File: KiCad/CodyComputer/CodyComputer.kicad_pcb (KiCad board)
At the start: 2 copper layers, 160 x 100 mm, 59 parts, among them J1 Barrel_Jack, J2 Power LED, J3 PropPlug, J4 Video Out, J5 Audio Out, J6 Cody Expansion/Cartridge Port, J7 Keyboard Connector, J8 Joystick 1, J9 Joystick 2, U1 74HC541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

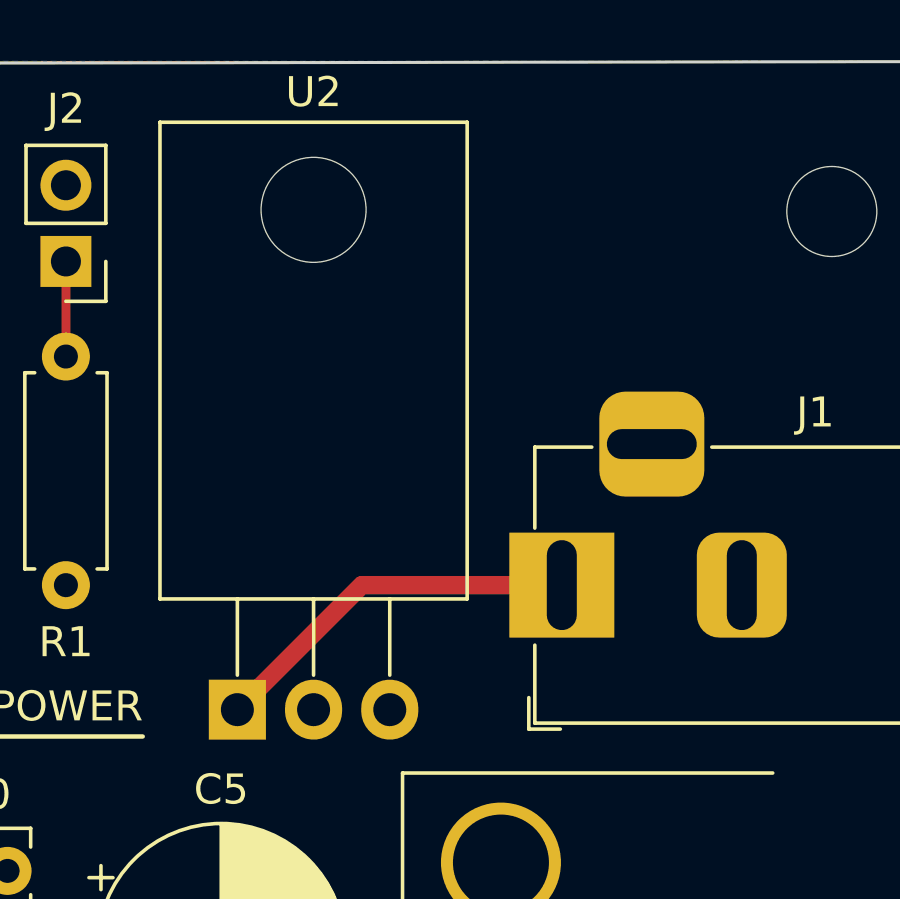
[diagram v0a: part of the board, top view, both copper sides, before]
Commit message: Add debug power connector to PCB
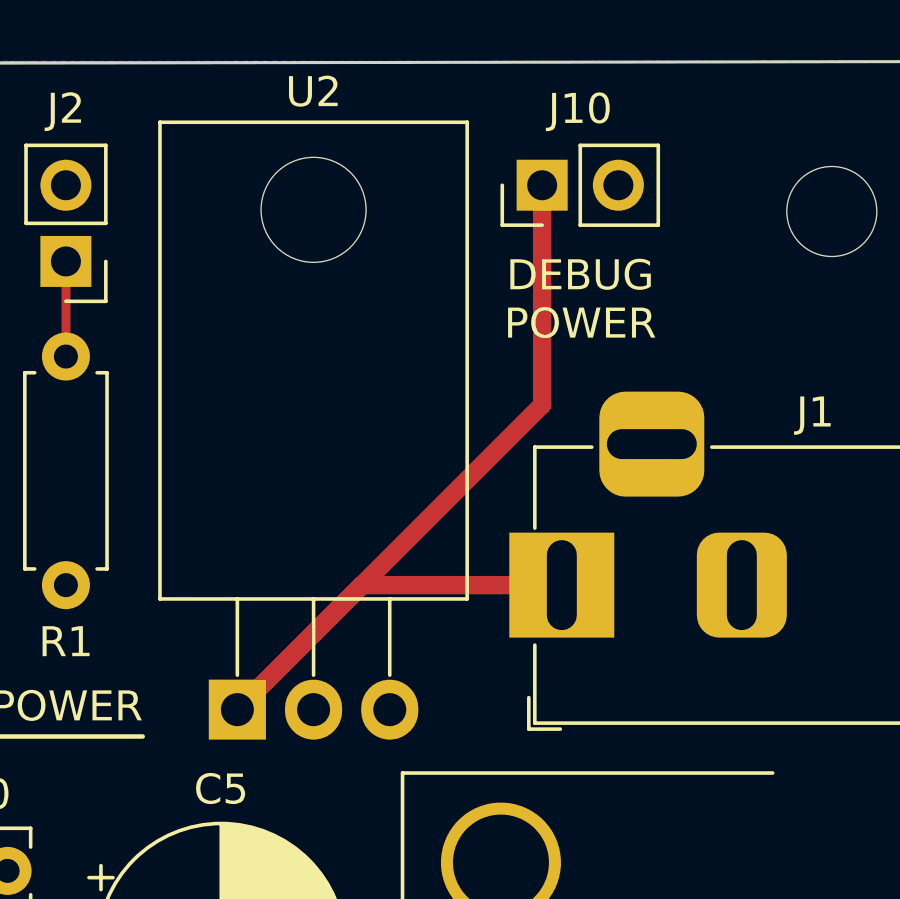
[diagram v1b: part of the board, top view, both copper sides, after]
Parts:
- added J10: Debug Power (Do Not Populate), Connector_PinHeader_2.54mm:PinHeader_1x02_P2.54mm_Vertical, F.Cu at (203.8, 51.4)
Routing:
- net /Propeller, Video, Audio, Power/VIN: track 12.5 -> 34.2 mm
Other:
- board text added: "DEBUG POWER"
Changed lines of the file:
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@@
     )
   )
+  (footprint "Connector_PinHeader_2.54mm:PinHeader_1x02_P2.54mm_Vertical" (layer "F.Cu")
+    (at 203.835 51.435 90)
+    (descr "Through hole straight pin header, 1x02, 2.54mm pitch, single row")
+    (tags "Through hole pin header THT 1x02 2.54mm single row")
+    (property "Sheetfile" "Propeller.kicad_sch")
+    (property "Sheetname" "Propeller, Video, Audio, Power")
+    (attr through_hole)
+    (fp_text reference "J10" (at 2.54 1.27 180) (layer "F.SilkS")
+      (effects (font (size 1 1) (thickness 0.15)))
+    )
+    (fp_text value "Debug Power (Do Not Populate)" (at -2.286 0.005 180) (layer "F.Fab")
+      (effects (font (size 1 1) (thickness 0.15)))
+    )
+    (fp_text user "${REFERENCE}" (at 0 1.27) (layer "F.Fab")
+      (effects (font (size 1 1) (thickness 0.15)))
+    )
+    (fp_line (start -1.33 1.27) (end 1.33 1.27) (layer "F.SilkS") (width 0.12))
+    (fp_line (start -1.33 3.87) (end 1.33 3.87) (layer "F.SilkS") (width 0.12))
+    (fp_line (start -1.33 -1.33) (end 0 -1.33) (layer "F.SilkS") (width 0.12))
+    (fp_line (start -1.33 0) (end -1.33 -1.33) (layer "F.SilkS") (width 0.12))
+    (fp_line (start -1.33 1.27) (end -1.33 3.87) (layer "F.SilkS") (width 0.12))
+    (fp_line (start 1.33 1.27) (end 1.33 3.87) (layer "F.SilkS") (width 0.12))
+    (fp_line (start 1.8 -1.8) (end -1.8 -1.8) (layer "F.CrtYd") (width 0.05))
+    (fp_line (start -1.8 -1.8) (end -1.8 4.35) (layer "F.CrtYd") (width 0.05))
+    (fp_line (start -1.8 4.35) (end 1.8 4.35) (layer "F.CrtYd") (width 0.05))
+    (fp_line (start 1.8 4.35) (end 1.8 -1.8) (layer "F.CrtYd") (width 0.05))
+    (fp_line (start -1.27 3.81) (end -1.27 -0.635) (layer "F.Fab") (width 0.1))
+    (fp_line (start -1.27 -0.635) (end -0.635 -1.27) (layer "F.Fab") (width 0.1))
+    (fp_line (start 1.27 -1.27) (end 1.27 3.81) (layer "F.Fab") (width 0.1))
+    (fp_line (start -0.635 -1.27) (end 1.27 -1.27) (layer "F.Fab") (width 0.1))
+    (fp_line (start 1.27 3.81) (end -1.27 3.81) (layer "F.Fab") (width 0.1))
+    (pad "1" thru_hole rect (at 0 0 90) (size 1.7 1.7) (drill 1) (layers *.Cu *.Mask)
+      (net 54 "/Propeller, Video, Audio, Power/VIN") (pinfunction "Pin_1") (pintype "passive"))
+    (pad "2" thru_hole oval (at 0 2.54 90) (size 1.7 1.7) (drill 1) (layers *.Cu *.Mask)
+      (net 16 "GND") (pinfunction "Pin_2") (pintype "passive"))
+    (model "${KICAD6_3DMODEL_DIR}/Connector_PinHeader_2.54mm.3dshapes/PinHeader_1x02_P2.54mm_Vertical.wrl"
+      (offset (xyz 0 0 0))
+      (scale (xyz 1 1 1))
+      (rotate (xyz 0 0 0))
+    )
+  )
   (footprint "Diode_THT:D_DO-34_SOD68_P7.62mm_Horizontal" (layer "F.Cu")
     (at 196.855 97.53425 180)
@@
     (fp_line (start 6.63 0) (end 5.45 0) (layer "F.SilkS") (width 0.12))
     (fp_line (start 2.866 -0.92) (end 2.866 0.92) (layer "F.SilkS") (width 0.12))
+    (fp_line (start 8.63 -1.05) (end -1 -1.05) (layer "F.CrtYd") (width 0.05))
+    (fp_line (start -1 1.05) (end 8.63 1.05) (layer "F.CrtYd") (width 0.05))
     (fp_line (start -1 -1.05) (end -1 1.05) (layer "F.CrtYd") (width 0.05))
     (fp_line (start 8.63 1.05) (end 8.63 -1.05) (layer "F.CrtYd") (width 0.05))
-    (fp_line (start -1 1.05) (end 8.63 1.05) (layer "F.CrtYd") (width 0.05))
-    (fp_line (start 8.63 -1.05) (end -1 -1.05) (layer "F.CrtYd") (width 0.05))
     (fp_line (start 5.33 -0.8) (end 2.29 -0.8) (layer "F.Fab") (width 0.1))
-    (fp_line (start 2.846 -0.8) (end 2.846 0.8) (layer "F.Fab") (width 0.1))
+    (fp_line (start 2.29 0.8) (end 5.33 0.8) (layer "F.Fab") (width 0.1))
     (fp_line (start 5.33 0.8) (end 5.33 -0.8) (layer "F.Fab") (width 0.1))
     (fp_line (start 2.29 -0.8) (end 2.29 0.8) (layer "F.Fab") (width 0.1))
-    (fp_line (start 2.29 0.8) (end 5.33 0.8) (layer "F.Fab") (width 0.1))
     (fp_line (start 7.62 0) (end 5.33 0) (layer "F.Fab") (width 0.1))
     (fp_line (start 2.746 -0.8) (end 2.746 0.8) (layer "F.Fab") (width 0.1))
+    (fp_line (start 2.846 -0.8) (end 2.846 0.8) (layer "F.Fab") (width 0.1))
     (fp_line (start 0 0) (end 2.29 0) (layer "F.Fab") (width 0.1))
     (fp_line (start 2.646 -0.8) (end 2.646 0.8) (layer "F.Fab") (width 0.1))
@@
     (effects (font (size 1 1) (thickness 0.15)))
   )
+  (gr_text "DEBUG\nPOWER" (at 205.105 55.245) (layer "F.SilkS")
+    (effects (font (size 1 1) (thickness 0.15)))
+  )
   (gr_text "AUDIO/VIDEO" (at 70.99 128.81) (layer "F.SilkS")
     (effects (font (size 1 1) (thickness 0.15)))
@@
   (segment (start 103.49 126.36) (end 98.806 126.36) (width 0.3048) (layer "B.Cu") (net 53))
   (arc (start 103.49 126.36) (mid 104.197107 126.067107) (end 104.49 125.36) (width 0.3048) (layer "B.Cu") (net 53))
+  (segment (start 203.835 51.435) (end 203.835 58.755) (width 0.6096) (layer "F.Cu") (net 54))
   (segment (start 193.675 68.915) (end 197.82625 64.76375) (width 0.6096) (layer "F.Cu") (net 54))
   (segment (start 197.82625 64.76375) (end 204.49 64.76375) (width 0.6096) (layer "F.Cu") (net 54))
+  (segment (start 203.835 58.755) (end 193.675 68.915) (width 0.6096) (layer "F.Cu") (net 54))
   (segment (start 83.82 59.32) (end 83.82 58.78) (width 0.3048) (layer "F.Cu") (net 55))
   (segment (start 80.56055 60.32) (end 82.82 60.32) (width 0.3048) (layer "F.Cu") (net 55))
@@
     )
   )
+  (group "" (id 8f27f4a9-caed-4a92-b022-43b832c1351f)
+    (members
+      30f09286-95d4-4c05-bd76-673c05b0e06d
+    )
+  )

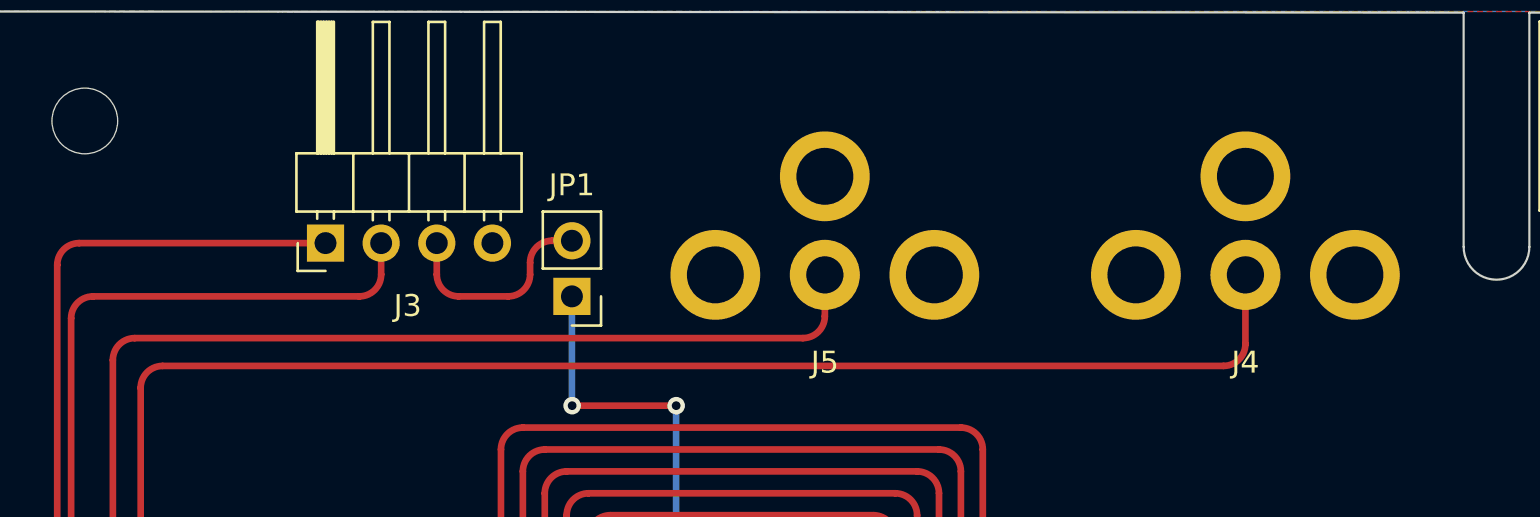
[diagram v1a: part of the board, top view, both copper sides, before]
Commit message: Move RCA connectors by additional 0.4mm
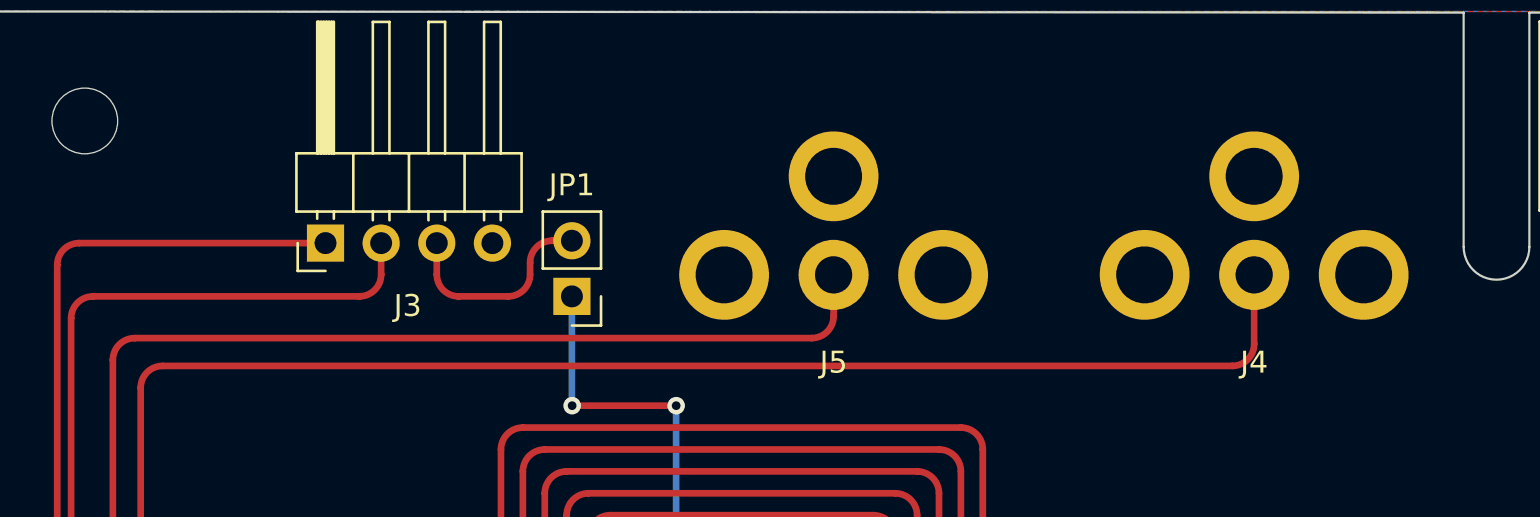
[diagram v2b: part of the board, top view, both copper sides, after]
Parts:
- moved J4 0.40 mm to (116.9, 59.3)
- moved J5 0.40 mm to (97.7, 59.3)
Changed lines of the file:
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@@
       (effects (font (size 1 1) (thickness 0.15)))
     )
+    (fp_line (start -1.33 -1.33) (end 0 -1.33) (layer "F.SilkS") (width 0.12))
+    (fp_line (start -1.33 3.87) (end 1.33 3.87) (layer "F.SilkS") (width 0.12))
+    (fp_line (start -1.33 1.27) (end -1.33 3.87) (layer "F.SilkS") (width 0.12))
     (fp_line (start -1.33 1.27) (end 1.33 1.27) (layer "F.SilkS") (width 0.12))
-    (fp_line (start -1.33 3.87) (end 1.33 3.87) (layer "F.SilkS") (width 0.12))
-    (fp_line (start -1.33 -1.33) (end 0 -1.33) (layer "F.SilkS") (width 0.12))
     (fp_line (start -1.33 0) (end -1.33 -1.33) (layer "F.SilkS") (width 0.12))
-    (fp_line (start -1.33 1.27) (end -1.33 3.87) (layer "F.SilkS") (width 0.12))
     (fp_line (start 1.33 1.27) (end 1.33 3.87) (layer "F.SilkS") (width 0.12))
     (fp_line (start 1.8 -1.8) (end -1.8 -1.8) (layer "F.CrtYd") (width 0.05))
@@
     (fp_line (start -1 6.75) (end -5 6.75) (layer "F.CrtYd") (width 0.05))
     (fp_line (start -14 4.75) (end -14 -4.75) (layer "F.CrtYd") (width 0.05))
+    (fp_line (start 1 -4.5) (end 1 -4.75) (layer "F.CrtYd") (width 0.05))
     (fp_line (start 1 -4.5) (end 1 -2) (layer "F.CrtYd") (width 0.05))
     (fp_line (start 1 -2) (end 2 -2) (layer "F.CrtYd") (width 0.05))
-    (fp_line (start 1 -4.5) (end 1 -4.75) (layer "F.CrtYd") (width 0.05))
     (fp_line (start -1 4.75) (end -1 6.75) (layer "F.CrtYd") (width 0.05))
     (fp_line (start -10.2 -4.5) (end -10.2 4.5) (layer "F.Fab") (width 0.1))
@@
   )
   (footprint "Cody_Components:CodyRCAJack" (layer "F.Cu")
-    (at 116.48035 59.3378)
+    (at 116.88035 59.3378)
     (descr "RCA audio/video jack modeled after the CUI RCJ-01X part series. Pin numbers are swapped to match KiCad's coaxial connector symbols.")
     (property "Sheetfile" "Propeller.kicad_sch")
@@
   )
   (footprint "Cody_Components:CodyRCAJack" (layer "F.Cu")
-    (at 97.27795 59.3378)
+    (at 97.67795 59.3378)
     (descr "RCA audio/video jack modeled after the CUI RCJ-01X part series. Pin numbers are swapped to match KiCad's coaxial connector symbols.")
     (property "Sheetfile" "Propeller.kicad_sch")
@@
   (segment (start 207.01 137.79) (end 207.01 86.1275) (width 0.3048) (layer "B.Cu") (net 91))
   (arc (start 207.01 86.1275) (mid 206.717107 85.420393) (end 206.01 85.1275) (width 0.3048) (layer "B.Cu") (net 91))
-  (segment (start 67.04 63.495) (end 115.48035 63.495) (width 0.3048) (layer "F.Cu") (net 92))
+  (segment (start 66.04 107.072) (end 66.04 64.495) (width 0.3048) (layer "F.Cu") (net 92))
   (segment (start 68.58 108.072) (end 68.58 115.184) (width 0.3048) (layer "F.Cu") (net 92))
-  (segment (start 66.04 107.072) (end 66.04 64.495) (width 0.3048) (layer "F.Cu") (net 92))
   (segment (start 68.58 108.072) (end 67.04 108.072) (width 0.3048) (layer "F.Cu") (net 92))
-  (segment (start 116.48035 62.495) (end 116.48035 59.3378) (width 0.3048) (layer "F.Cu") (net 92))
+  (segment (start 116.88035 62.495) (end 116.88035 59.3378) (width 0.3048) (layer "F.Cu") (net 92))
+  (segment (start 67.04 63.495) (end 115.88035 63.495) (width 0.3048) (layer "F.Cu") (net 92))
   (arc (start 66.04 64.495) (mid 66.332893 63.787893) (end 67.04 63.495) (width 0.3048) (layer "F.Cu") (net 92))
+  (arc (start 115.88035 63.495) (mid 116.587457 63.202107) (end 116.88035 62.495) (width 0.3048) (layer "F.Cu") (net 92))
   (arc (start 67.04 108.072) (mid 66.332893 107.779107) (end 66.04 107.072) (width 0.3048) (layer "F.Cu") (net 92))
-  (arc (start 115.48035 63.495) (mid 116.187457 63.202107) (end 116.48035 62.495) (width 0.3048) (layer "F.Cu") (net 92))
-  (segment (start 97.27795 61.225) (end 97.27795 59.3378) (width 0.3048) (layer "F.Cu") (net 93))
+  (segment (start 97.67795 61.225) (end 97.67795 59.3378) (width 0.3048) (layer "F.Cu") (net 93))
+  (segment (start 65.77 62.225) (end 96.67795 62.225) (width 0.3048) (layer "F.Cu") (net 93))
+  (segment (start 64.77 73.02) (end 64.77 63.225) (width 0.3048) (layer "F.Cu") (net 93))
   (segment (start 64.77 124.82) (end 64.77 70.48) (width 0.3048) (layer "F.Cu") (net 93))
   (segment (start 68.58 125.82) (end 65.77 125.82) (width 0.3048) (layer "F.Cu") (net 93))
-  (segment (start 64.77 73.02) (end 64.77 63.225) (width 0.3048) (layer "F.Cu") (net 93))
-  (segment (start 65.77 62.225) (end 96.27795 62.225) (width 0.3048) (layer "F.Cu") (net 93))
   (arc (start 64.77 63.225) (mid 65.062893 62.517893) (end 65.77 62.225) (width 0.3048) (layer "F.Cu") (net 93))
-  (arc (start 96.27795 62.225) (mid 96.985057 61.932107) (end 97.27795 61.225) (width 0.3048) (layer "F.Cu") (net 93))
+  (arc (start 96.67795 62.225) (mid 97.385057 61.932107) (end 97.67795 61.225) (width 0.3048) (layer "F.Cu") (net 93))
   (arc (start 64.77 124.82) (mid 65.062893 125.527107) (end 65.77 125.82) (width 0.3048) (layer "F.Cu") (net 93))
   (segment (start 68.58 118.74) (end 68.58 123.82) (width 0.3048) (layer "F.Cu") (net 94))
